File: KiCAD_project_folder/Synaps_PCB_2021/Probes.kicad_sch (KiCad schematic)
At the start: 0 parts

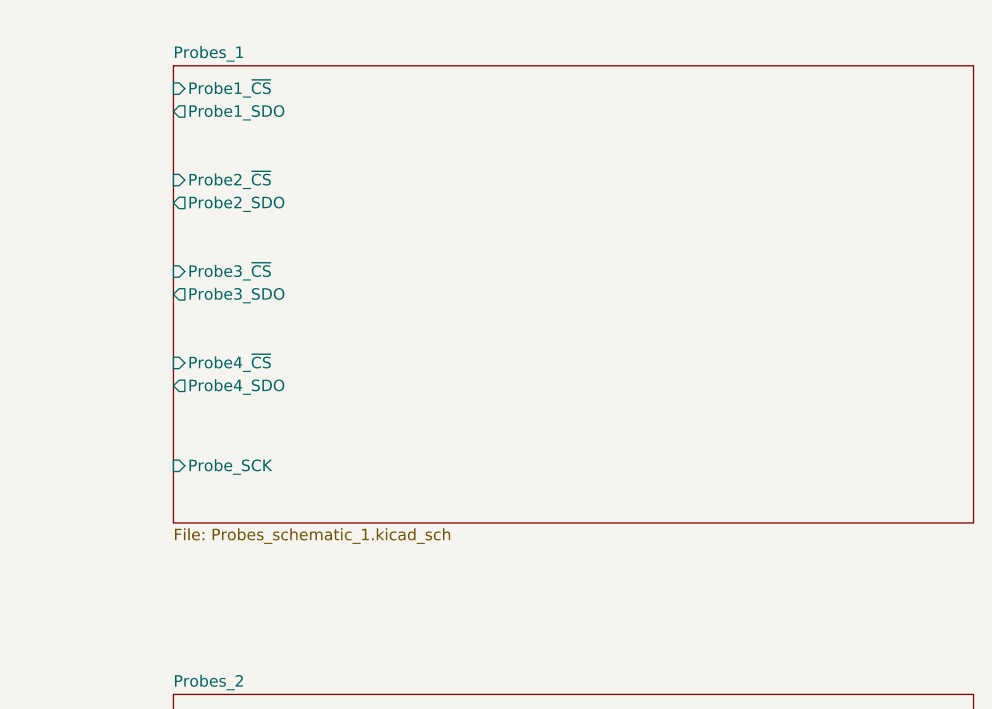
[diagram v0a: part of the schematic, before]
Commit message: Added Esp32-S2 datasheet files and hardware design guidelines to project
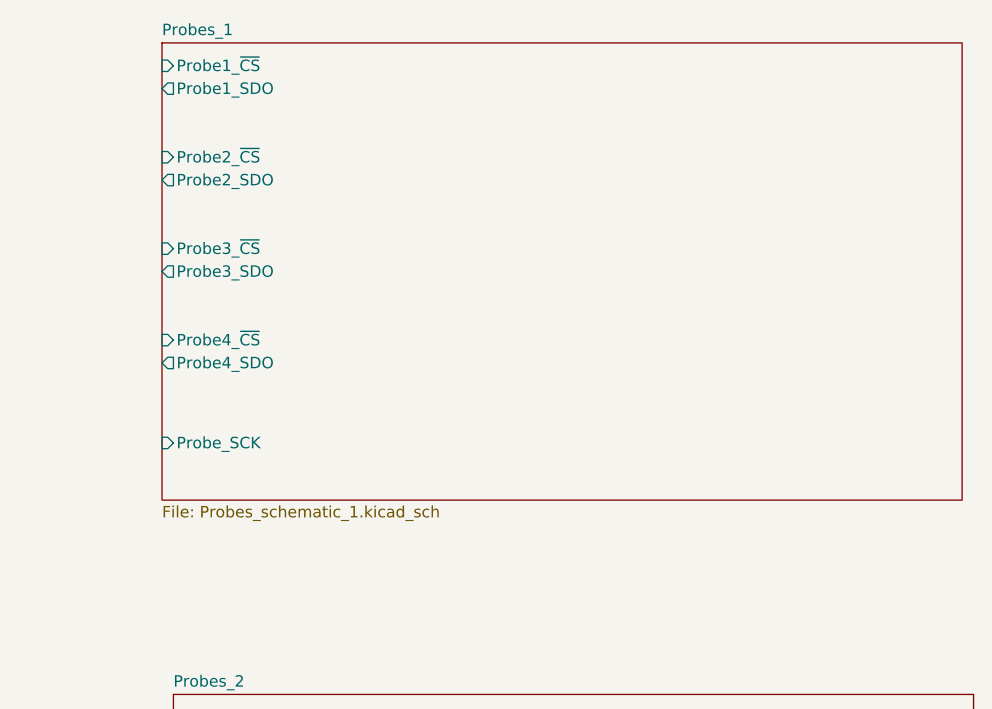
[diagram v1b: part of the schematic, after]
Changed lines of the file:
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@@
     (effects (font (size 1.27 1.27)) (justify right))
   )
-  (sheet (at 177.8 24.13) (size 88.9 50.8) (fields_autoplaced)
+  (sheet (at 176.53 21.59) (size 88.9 50.8) (fields_autoplaced)
     (stroke (width 0) (type solid) (color 0 0 0 0))
     (fill (color 0 0 0 0.0000))
-    (property "Sheet name" "Probes_1" (id 0) (at 177.8 23.4184 0)
+    (property "Sheet name" "Probes_1" (id 0) (at 176.53 20.8784 0)
       (effects (font (size 1.27 1.27)) (justify left bottom))
     )
-    (property "Sheet file" "Probes_schematic_1.kicad_sch" (id 1) (at 177.8 75.5146 0)
+    (property "Sheet file" "Probes_schematic_1.kicad_sch" (id 1) (at 176.53 72.9746 0)
       (effects (font (size 1.27 1.27)) (justify left top))
     )
-    (pin "Probe1_~{CS}" input (at 177.8 26.67 180)
+    (pin "Probe1_~{CS}" input (at 176.53 24.13 180)
       (effects (font (size 1.27 1.27)) (justify left))
     )
-    (pin "Probe2_~{CS}" input (at 177.8 36.83 180)
+    (pin "Probe2_~{CS}" input (at 176.53 34.29 180)
       (effects (font (size 1.27 1.27)) (justify left))
     )
-    (pin "Probe3_~{CS}" input (at 177.8 46.99 180)
+    (pin "Probe3_~{CS}" input (at 176.53 44.45 180)
       (effects (font (size 1.27 1.27)) (justify left))
     )
-    (pin "Probe4_~{CS}" input (at 177.8 57.15 180)
+    (pin "Probe4_~{CS}" input (at 176.53 54.61 180)
       (effects (font (size 1.27 1.27)) (justify left))
     )
-    (pin "Probe1_SDO" output (at 177.8 29.21 180)
+    (pin "Probe1_SDO" output (at 176.53 26.67 180)
       (effects (font (size 1.27 1.27)) (justify left))
     )
-    (pin "Probe2_SDO" output (at 177.8 39.37 180)
+    (pin "Probe2_SDO" output (at 176.53 36.83 180)
       (effects (font (size 1.27 1.27)) (justify left))
     )
-    (pin "Probe3_SDO" output (at 177.8 49.53 180)
+    (pin "Probe3_SDO" output (at 176.53 46.99 180)
       (effects (font (size 1.27 1.27)) (justify left))
     )
-    (pin "Probe4_SDO" output (at 177.8 59.69 180)
+    (pin "Probe4_SDO" output (at 176.53 57.15 180)
       (effects (font (size 1.27 1.27)) (justify left))
     )
-    (pin "Probe_SCK" input (at 177.8 68.58 180)
+    (pin "Probe_SCK" input (at 176.53 66.04 180)
       (effects (font (size 1.27 1.27)) (justify left))
     )

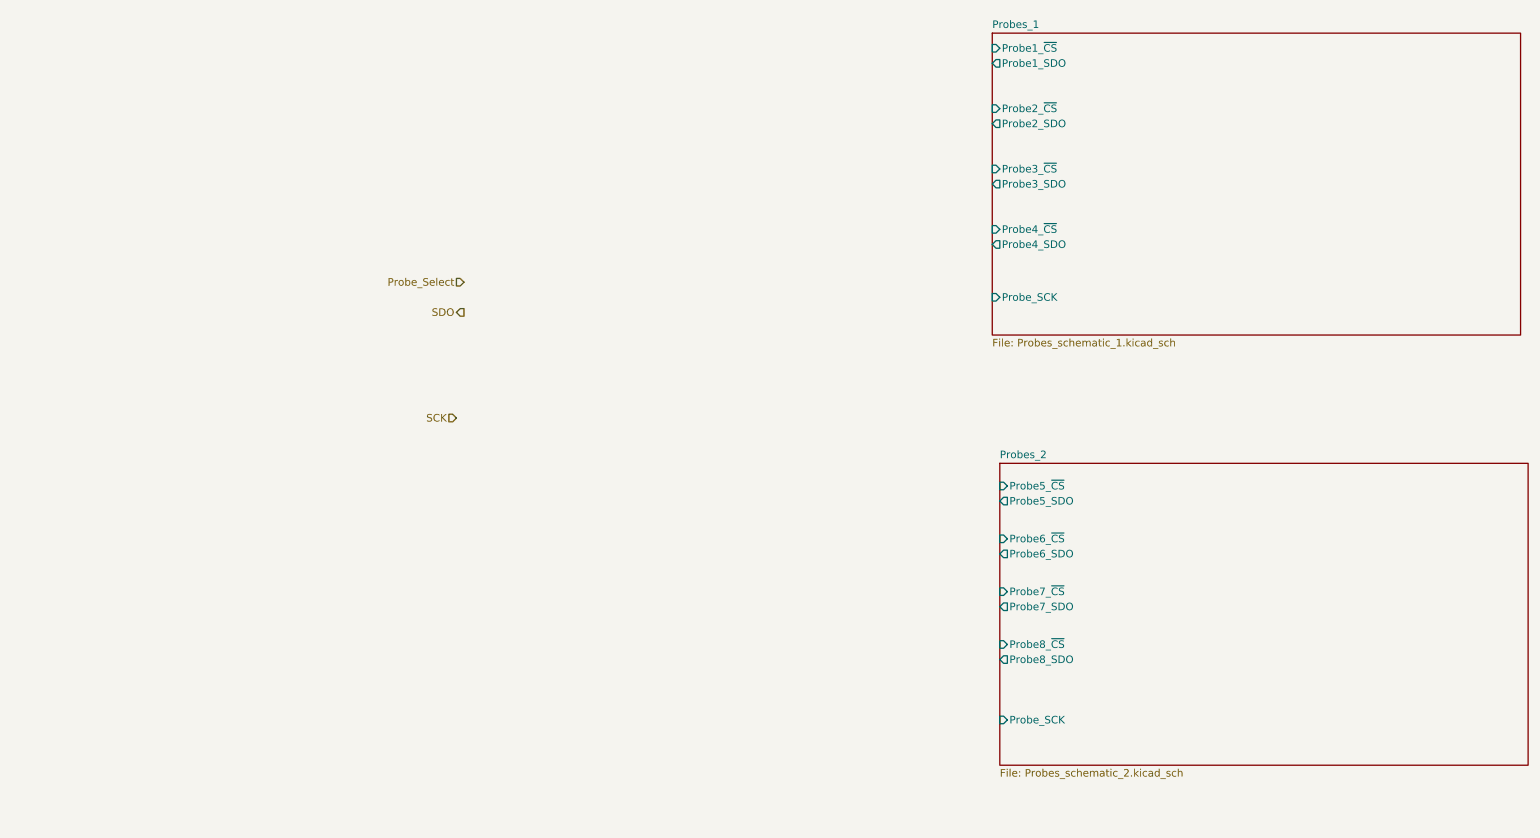
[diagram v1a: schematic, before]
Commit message: Reworded PMIC and probe select
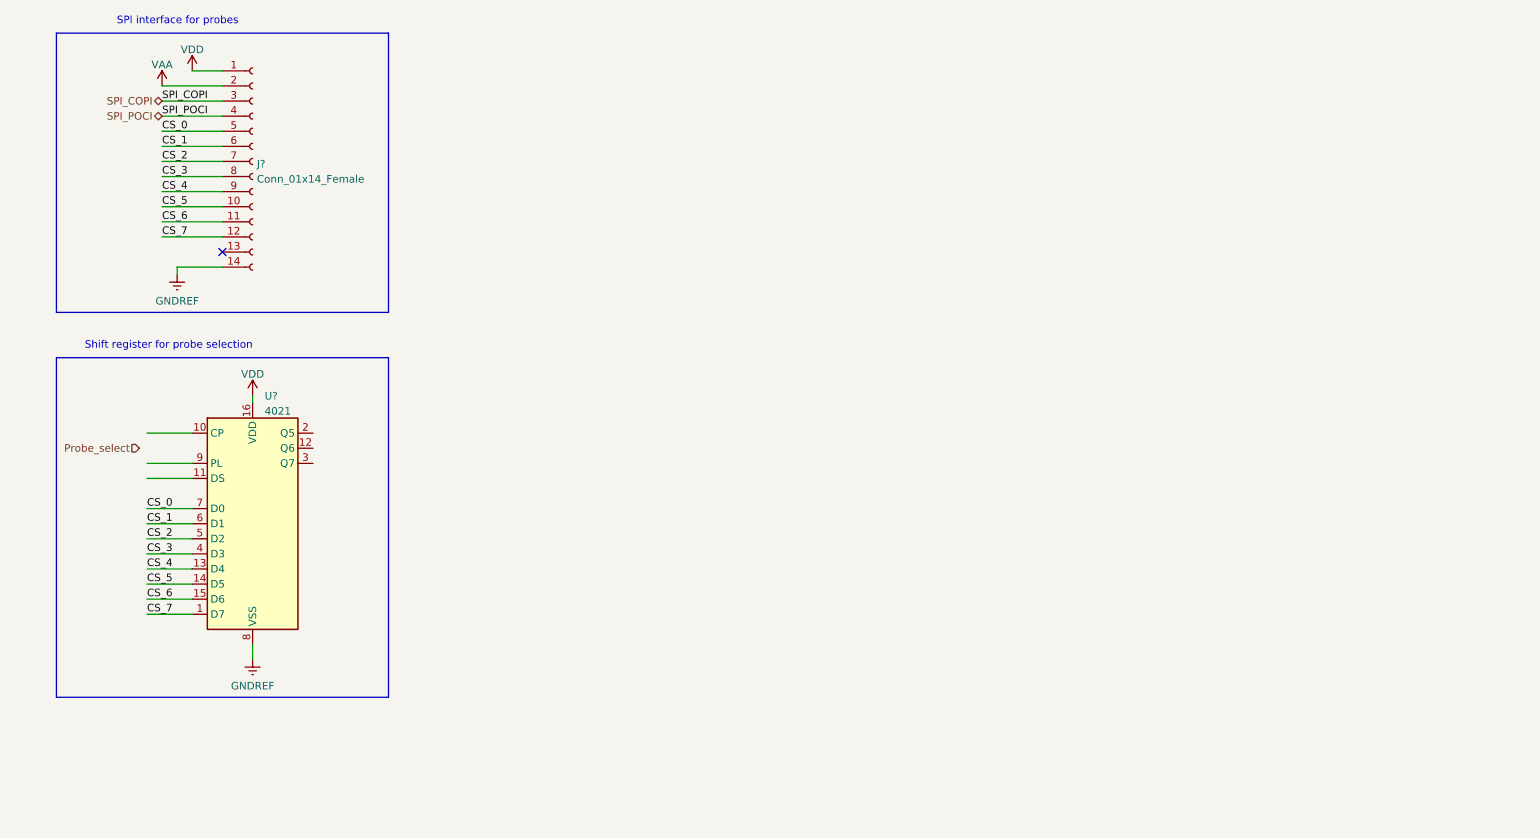
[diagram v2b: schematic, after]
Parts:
- added J?: Conn_01x14_Female, symbol Connector:Conn_01x14_Female
- added U?: 4021, symbol 4xxx:4021
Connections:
- new net CS_0: J?.5 (Pin_5), U?.7 (D0)
- new net CS_1: J?.6 (Pin_6), U?.6 (D1)
- new net CS_2: J?.7 (Pin_7), U?.5 (D2)
- new net CS_3: J?.8 (Pin_8), U?.4 (D3)
- new net CS_4: J?.9 (Pin_9), U?.13 (D4)
- new net CS_5: J?.10 (Pin_10), U?.14 (D5)
- new net CS_6: J?.11 (Pin_11), U?.15 (D6)
- new net CS_7: J?.12 (Pin_12), U?.1 (D7)
- new net GNDREF: J?.14 (Pin_14), U?.8 (VSS)
- new net SPI_COPI: J?.3 (Pin_3)
- new net SPI_POCI: J?.4 (Pin_4)
- new net VAA: J?.2 (Pin_2)
- new net VDD: J?.1 (Pin_1), U?.16 (VDD)
- no-connect marks 0 -> 1
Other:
- removed sheet Probes_1
- removed sheet Probes_2
- note added: "SPI interface for probes"
- note added: "Shift register for probe selection"

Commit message: Redid schematic, fixed wrong setup
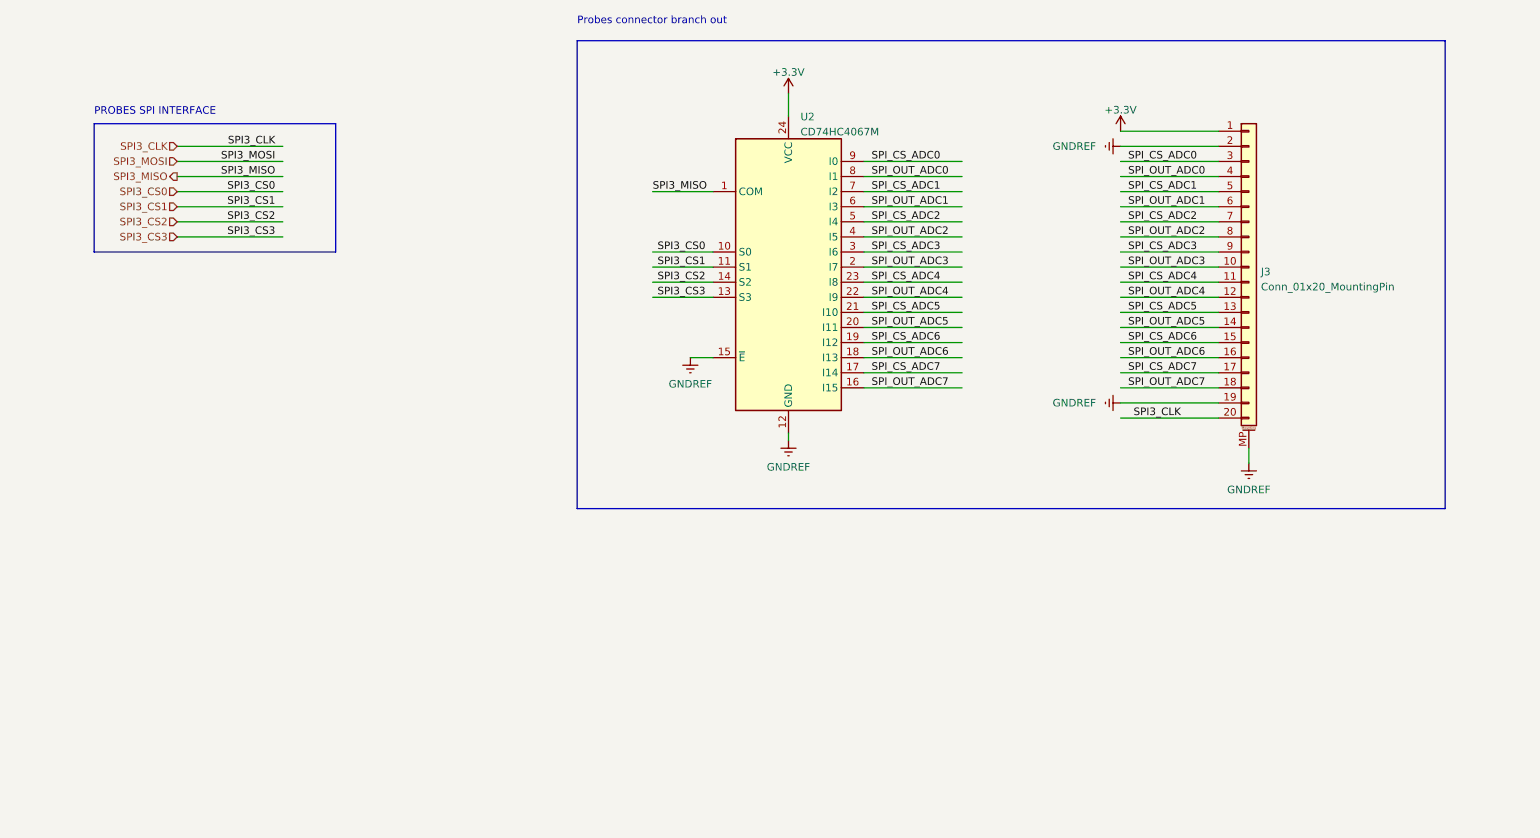
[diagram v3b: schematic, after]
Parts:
- removed J?: Conn_01x14_Female, symbol Connector:Conn_01x14_Female
- removed U?: 4021, symbol 4xxx:4021
- added J3: Conn_01x20_MountingPin, symbol Connector_Generic_MountingPin:Conn_01x20_MountingPin
- added U2: CD74HC4067M, Package_SO:SOIC-24W_7.5x15.4mm_P1.27mm, symbol 74xx:CD74HC4067M
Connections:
- net GNDREF: now also J3.19 (Pin_19), J3.2 (Pin_2), J3.MP (MountPin), U2.12 (GND), U2.15 (~{E})
- new net +3V3: J3.1 (Pin_1), U2.24 (VCC)
- new net SPI3_CLK: J3.20 (Pin_20)
- new net SPI3_CS0: U2.10 (S0)
- new net SPI3_CS1: U2.11 (S1)
- new net SPI3_CS2: U2.14 (S2)
- new net SPI3_CS3: U2.13 (S3)
- new net SPI3_MISO: U2.1 (COM)
- new net SPI_CS_ADC0: J3.3 (Pin_3), U2.9 (I0)
- new net SPI_CS_ADC1: J3.5 (Pin_5), U2.7 (I2)
- new net SPI_CS_ADC2: J3.7 (Pin_7), U2.5 (I4)
- new net SPI_CS_ADC3: J3.9 (Pin_9), U2.3 (I6)
- new net SPI_CS_ADC4: J3.11 (Pin_11), U2.23 (I8)
- new net SPI_CS_ADC5: J3.13 (Pin_13), U2.21 (I10)
- new net SPI_CS_ADC6: J3.15 (Pin_15), U2.19 (I12)
- new net SPI_CS_ADC7: J3.17 (Pin_17), U2.17 (I14)
- new net SPI_OUT_ADC0: J3.4 (Pin_4), U2.8 (I1)
- new net SPI_OUT_ADC1: J3.6 (Pin_6), U2.6 (I3)
- new net SPI_OUT_ADC2: J3.8 (Pin_8), U2.4 (I5)
- new net SPI_OUT_ADC3: J3.10 (Pin_10), U2.2 (I7)
- new net SPI_OUT_ADC4: J3.12 (Pin_12), U2.22 (I9)
- new net SPI_OUT_ADC5: J3.14 (Pin_14), U2.20 (I11)
- new net SPI_OUT_ADC6: J3.16 (Pin_16), U2.18 (I13)
- new net SPI_OUT_ADC7: J3.18 (Pin_18), U2.16 (I15)
- no-connect marks 1 -> 0
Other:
- note added: "PROBES SPI INTERFACE"
- note added: "Probes connector branch out"
- note removed: "SPI interface for probes"
- note removed: "Shift register for probe selection"

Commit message: Updated pcb editor with the new components imported
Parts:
- J3: footprint (none) -> Connector_PinHeader_2.00mm:PinHeader_1x20_P2.00mm_Vertical
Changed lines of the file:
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@@
       (effects (font (size 1.27 1.27)) (justify left))
     )
-    (property "Footprint" "" (id 2) (at 219.71 60.96 0)
+    (property "Footprint" "Connector_PinHeader_2.00mm:PinHeader_1x20_P2.00mm_Vertical" (id 2) (at 219.71 60.96 0)
       (effects (font (size 1.27 1.27)) hide)
     )

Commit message: Update schematic sheets and creates image to allow the board setup to be shared
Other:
- company: (none) -> Club SynapsÉTS
- title: (none) -> Misca PCB
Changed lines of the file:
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@@
 (kicad_sch (version 20211123) (generator eeschema)
   (paper "A4")
+  (title_block
+    (title "Misca PCB")
+    (date "2022-06-17")
+    (rev "A2")
+    (company "Club SynapsÉTS")
+    (comment 1 "Auteur : Jacques Veneziano")
+  )
   (wire (pts (xy 154.94 60.96) (xy 171.45 60.96))
     (stroke (width 0) (type default) (color 0 0 0 0))
